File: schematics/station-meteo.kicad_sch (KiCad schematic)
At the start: 4 parts, among them IC2 AHT20, U4 SCD40-D-R2

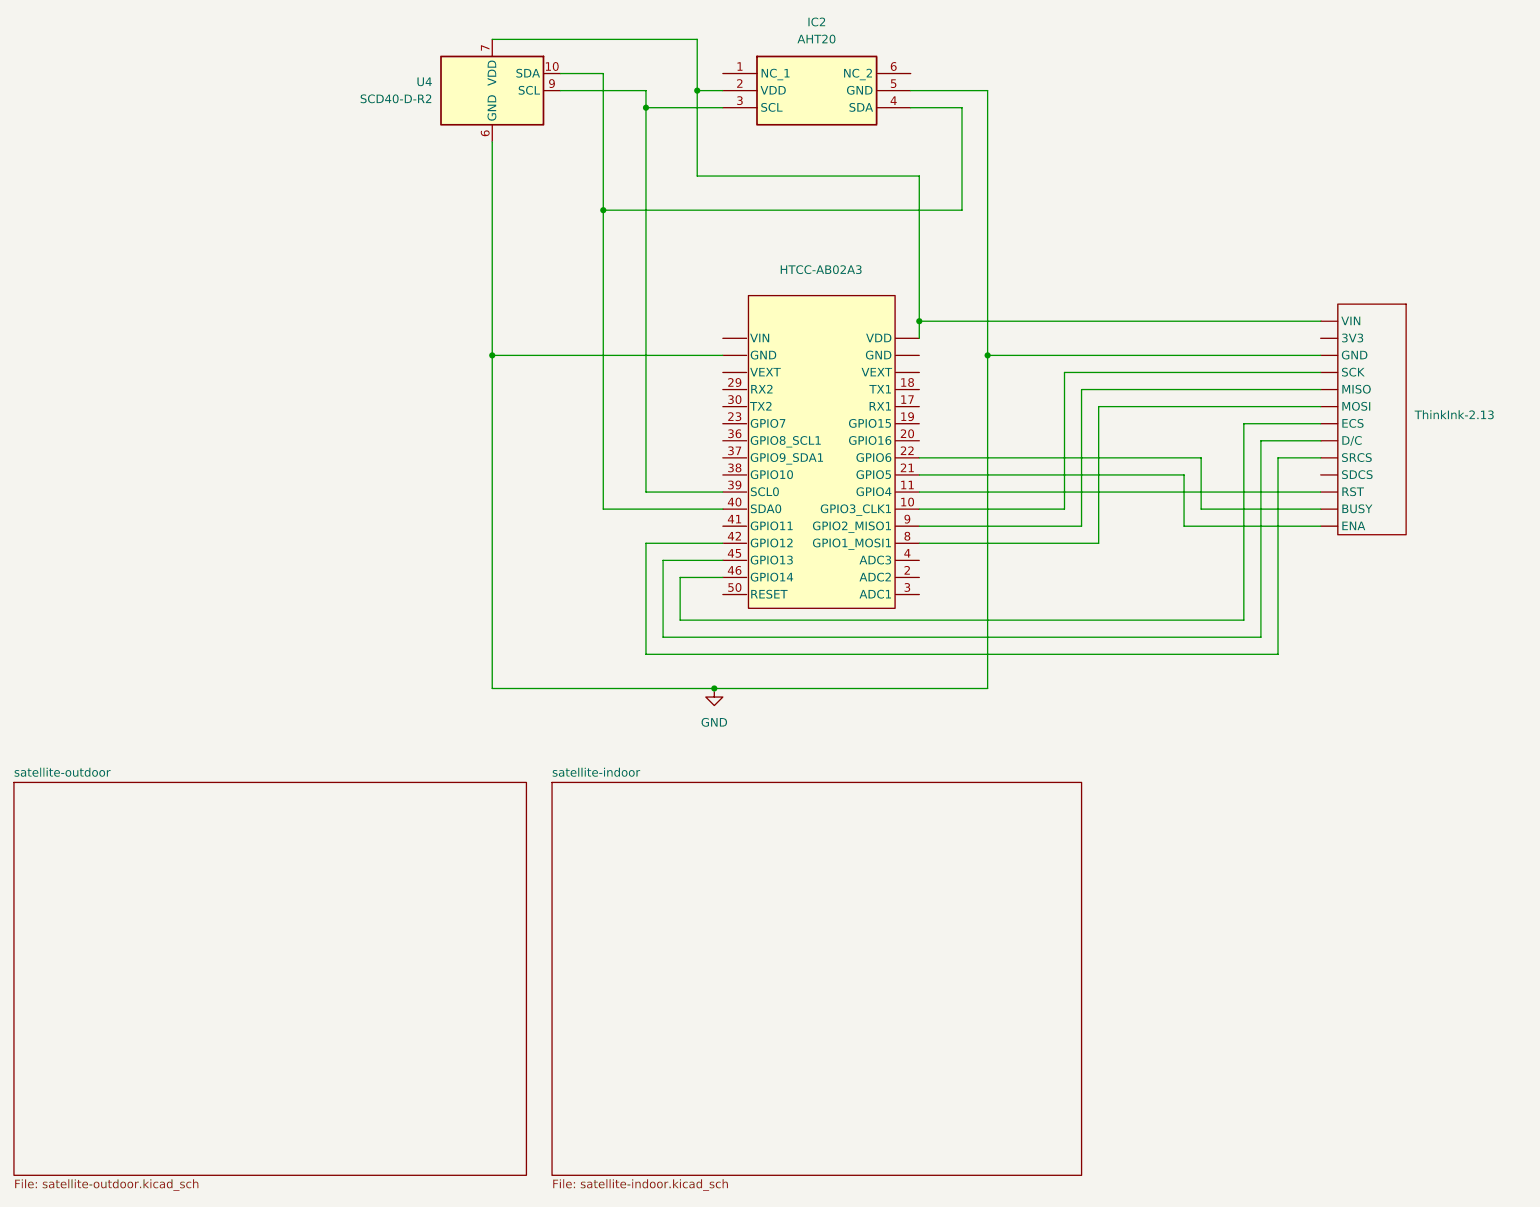
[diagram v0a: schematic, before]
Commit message: Schematics update: use Vext instead of VDD
Vext can be controllled and switched on/off.
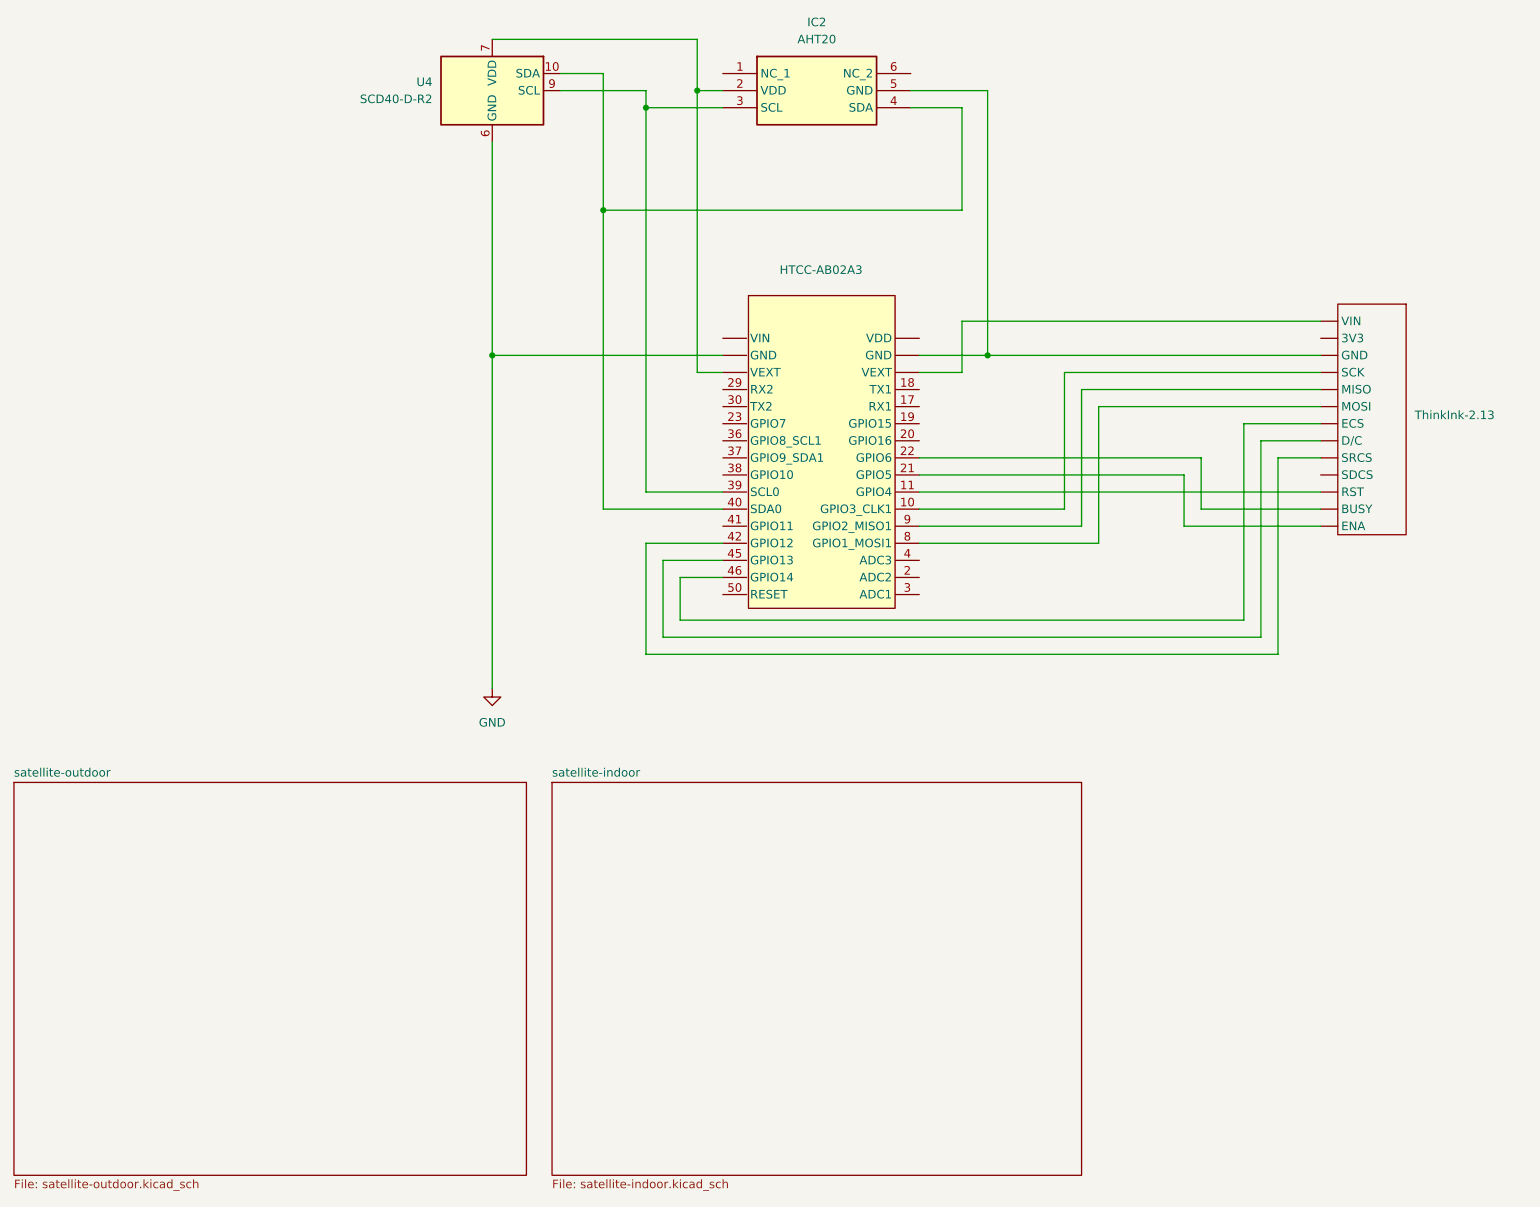
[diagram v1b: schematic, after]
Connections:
- net GND: no longer IC2.5 (GND), ThinkInk-2.13. (VIN)
- net at HTCC-AB02A3. (VIN), IC2.2 (VDD), U4.19 (VDD)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: no longer ThinkInk-2.13. (VIN)
- new net: HTCC-AB02A3. (VIN), ThinkInk-2.13. (VIN)
- new net: HTCC-AB02A3. (VIN), IC2.5 (GND), ThinkInk-2.13. (VIN)
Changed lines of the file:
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@@
-	)
-	(junction
-		(at 120.65 121.92)
-		(diameter 0)
-		(color 0 0 0 0)
-	)
-	(junction
-		(at 151.13 67.31)
-		(diameter 0)
-		(color 0 0 0 0)
 	)
 	(junction
@@
 	(wire
 		(pts
-			(xy 151.13 45.72) (xy 151.13 67.31)
-		)
-		(stroke
-			(width 0)
-			(type default)
-		)
-	)
-	(wire
-		(pts
-			(xy 151.13 67.31) (xy 210.82 67.31)
+			(xy 151.13 72.39) (xy 161.29 72.39)
 		)
 		(stroke
@@
 	(wire
 		(pts
+			(xy 157.48 67.31) (xy 210.82 67.31)
+		)
+		(stroke
+			(width 0)
+			(type default)
+		)
+	)
+	(wire
+		(pts
 			(xy 210.82 95.25) (xy 193.04 95.25)
 		)
@@
 	(wire
 		(pts
-			(xy 161.29 121.92) (xy 120.65 121.92)
-		)
-		(stroke
-			(width 0)
-			(type default)
-		)
-	)
-	(wire
-		(pts
 			(xy 113.03 114.3) (xy 201.93 114.3)
 		)
@@
 	(wire
 		(pts
+			(xy 118.11 33.02) (xy 118.11 74.93)
+		)
+		(stroke
+			(width 0)
+			(type default)
+		)
+	)
+	(wire
+		(pts
 			(xy 161.29 72.39) (xy 210.82 72.39)
 		)
@@
 	(wire
 		(pts
+			(xy 151.13 74.93) (xy 157.48 74.93)
+		)
+		(stroke
+			(width 0)
+			(type default)
+		)
+	)
+	(wire
+		(pts
 			(xy 210.82 87.63) (xy 204.47 87.63)
 		)
@@
 	(wire
 		(pts
-			(xy 151.13 45.72) (xy 118.11 45.72)
-		)
-		(stroke
-			(width 0)
-			(type default)
-		)
-	)
-	(wire
-		(pts
 			(xy 97.79 33.02) (xy 110.49 33.02)
 		)
@@
 	(wire
 		(pts
-			(xy 120.65 121.92) (xy 87.63 121.92)
-		)
-		(stroke
-			(width 0)
-			(type default)
-		)
-	)
-	(wire
-		(pts
-			(xy 118.11 45.72) (xy 118.11 33.02)
-		)
-		(stroke
-			(width 0)
-			(type default)
-		)
-	)
-	(wire
-		(pts
-			(xy 161.29 72.39) (xy 161.29 121.92)
-		)
-		(stroke
-			(width 0)
-			(type default)
-		)
-	)
-	(wire
-		(pts
 			(xy 104.14 95.25) (xy 121.92 95.25)
 		)
@@
 	(wire
 		(pts
-			(xy 151.13 67.31) (xy 151.13 69.85)
-		)
-		(stroke
-			(width 0)
-			(type default)
-		)
-	)
-	(wire
-		(pts
 			(xy 121.92 100.33) (xy 110.49 100.33)
 		)
@@
 	(wire
 		(pts
+			(xy 121.92 74.93) (xy 118.11 74.93)
+		)
+		(stroke
+			(width 0)
+			(type default)
+		)
+	)
+	(wire
+		(pts
 			(xy 177.8 100.33) (xy 177.8 80.01)
+		)
+		(stroke
+			(width 0)
+			(type default)
+		)
+	)
+	(wire
+		(pts
+			(xy 157.48 67.31) (xy 157.48 74.93)
 		)
 		(stroke
@@
 	(symbol
 		(lib_id "power:GND")
-		(at 120.65 121.92 0)
+		(at 87.63 121.92 0)
 		(unit 1)
 		(exclude_from_sim no)
@@
 		(fields_autoplaced yes)
 		(property "Reference" "#PWR03"
-			(at 120.65 128.27 0)
+			(at 87.63 128.27 0)
 			(effects
 				(font
@@
 		)
 		(property "Value" "GND"
-			(at 120.65 127 0)
+			(at 87.63 127 0)
 			(effects
 				(font
@@
 		)
 		(property "Footprint" ""
-			(at 120.65 121.92 0)
+			(at 87.63 121.92 0)
 			(effects
 				(font
@@
 		)
 		(property "Datasheet" ""
-			(at 120.65 121.92 0)
+			(at 87.63 121.92 0)
 			(effects
 				(font
@@
 		)
 		(property "Description" "Power symbol creates a global label with name \"GND\" , ground"
-			(at 120.65 121.92 0)
-			(effects
-				(font
+			(at 87.63 121.92 0)
+			(effects
+				(font

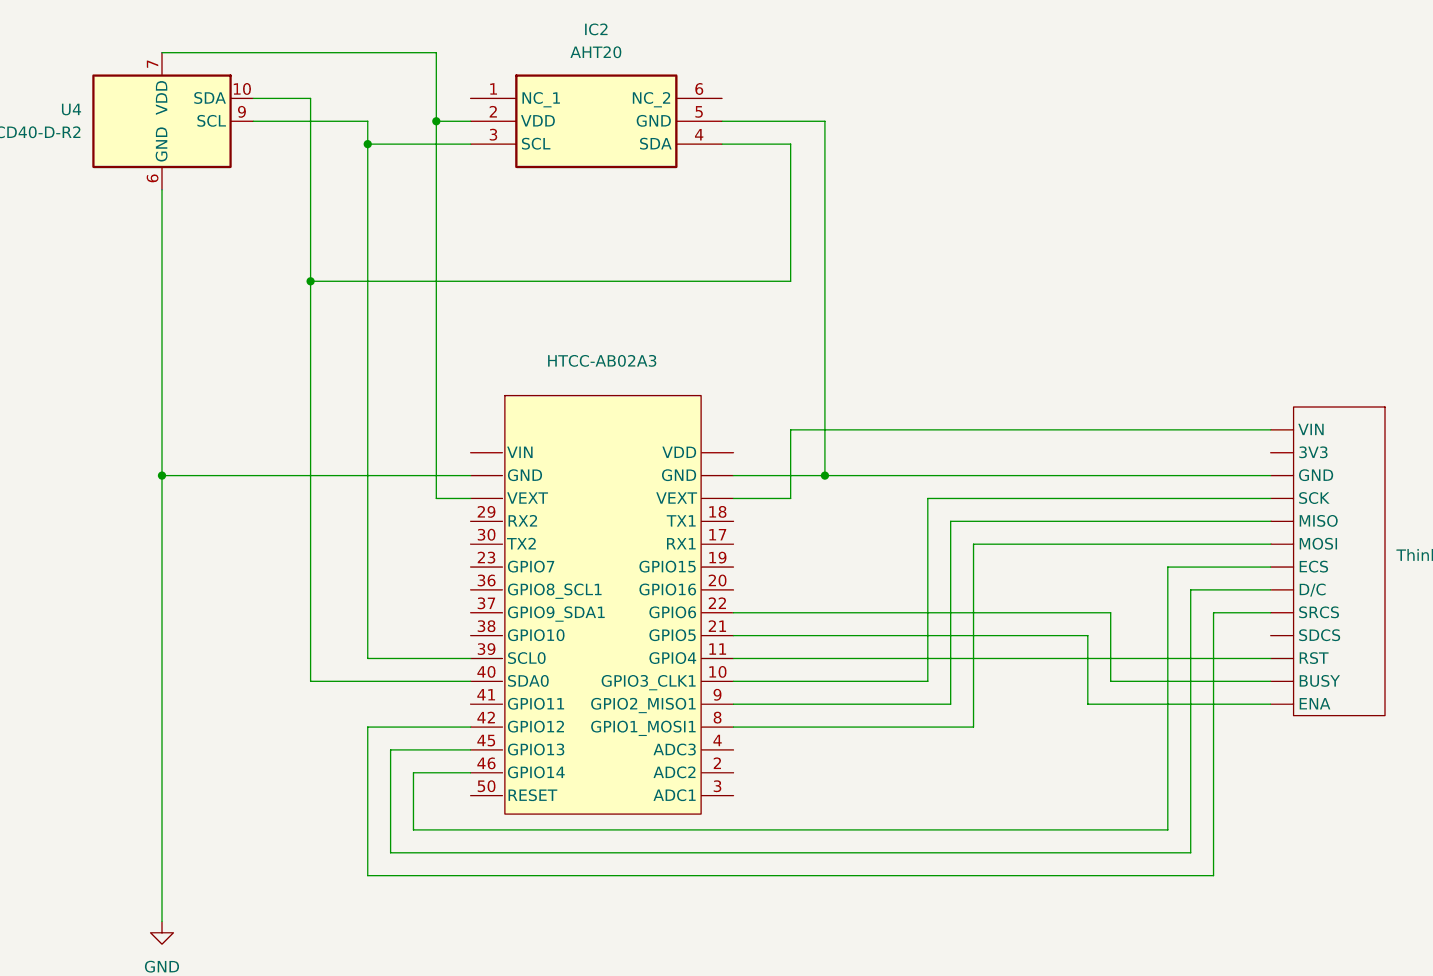
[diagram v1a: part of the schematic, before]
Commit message: Schematics/ add i2c pullups on outdoor sat.
20ko should do the trick.
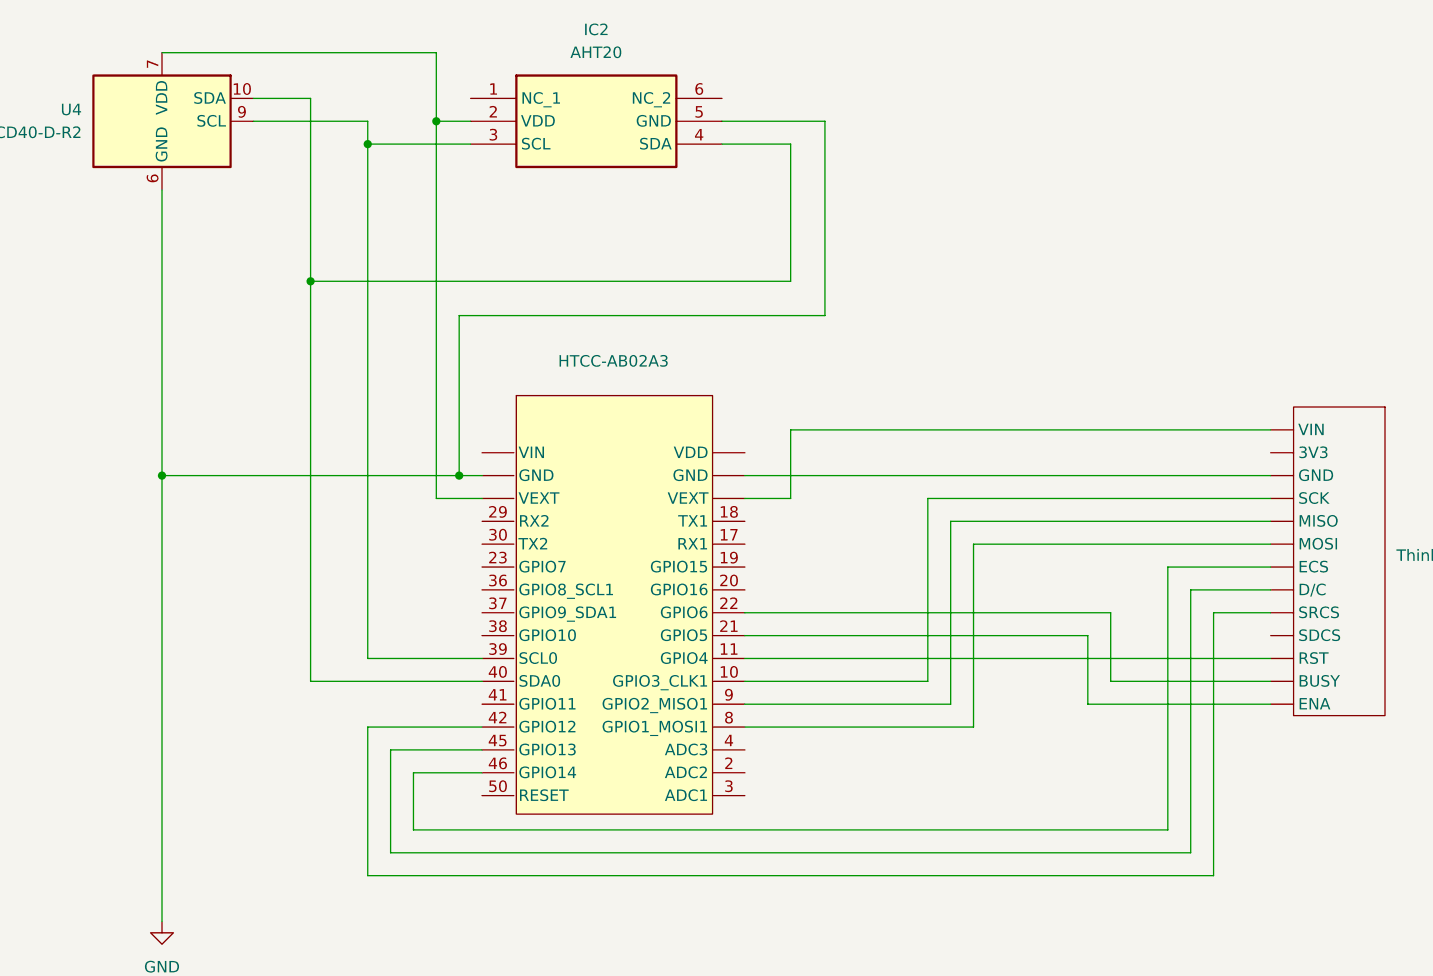
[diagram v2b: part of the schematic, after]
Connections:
- net GND: now also IC2.5 (GND)
- net at ThinkInk-2.13. (VIN): no longer HTCC-AB02A3. (VIN)
- new net: HTCC-AB02A3. (VIN), ThinkInk-2.13. (VIN) (x2)
- now unconnected: ThinkInk-2.13. (VIN)
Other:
- moved on the sheet: HTCC-AB02A3
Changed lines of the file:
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@@
+	)
+	(junction
+		(at 120.65 72.39)
+		(diameter 0)
+		(color 0 0 0 0)
 	)
 	(junction
@@
 		(color 0 0 0 0)
 	)
-	(junction
-		(at 161.29 72.39)
-		(diameter 0)
-		(color 0 0 0 0)
-	)
-	(wire
-		(pts
-			(xy 151.13 72.39) (xy 161.29 72.39)
-		)
-		(stroke
-			(width 0)
-			(type default)
-		)
-	)
 	(wire
 		(pts
@@
 	(wire
 		(pts
-			(xy 110.49 92.71) (xy 121.92 92.71)
+			(xy 110.49 92.71) (xy 123.19 92.71)
 		)
 		(stroke
@@
 	(wire
 		(pts
-			(xy 121.92 102.87) (xy 113.03 102.87)
+			(xy 123.19 102.87) (xy 113.03 102.87)
 		)
 		(stroke
@@
 	(wire
 		(pts
+			(xy 120.65 54.61) (xy 161.29 54.61)
+		)
+		(stroke
+			(width 0)
+			(type default)
+		)
+	)
+	(wire
+		(pts
 			(xy 157.48 50.8) (xy 104.14 50.8)
 		)
@@
 	(wire
 		(pts
-			(xy 193.04 87.63) (xy 151.13 87.63)
+			(xy 193.04 87.63) (xy 152.4 87.63)
 		)
 		(stroke
@@
 	(wire
 		(pts
-			(xy 161.29 72.39) (xy 210.82 72.39)
-		)
-		(stroke
-			(width 0)
-			(type default)
-		)
-	)
-	(wire
-		(pts
-			(xy 151.13 74.93) (xy 157.48 74.93)
+			(xy 152.4 72.39) (xy 210.82 72.39)
+		)
+		(stroke
+			(width 0)
+			(type default)
+		)
+	)
+	(wire
+		(pts
+			(xy 120.65 72.39) (xy 123.19 72.39)
+		)
+		(stroke
+			(width 0)
+			(type default)
+		)
+	)
+	(wire
+		(pts
+			(xy 120.65 72.39) (xy 120.65 54.61)
+		)
+		(stroke
+			(width 0)
+			(type default)
+		)
+	)
+	(wire
+		(pts
+			(xy 152.4 74.93) (xy 157.48 74.93)
 		)
 		(stroke
@@
 	(wire
 		(pts
-			(xy 151.13 97.79) (xy 175.26 97.79)
+			(xy 152.4 97.79) (xy 175.26 97.79)
 		)
 		(stroke
@@
 	(wire
 		(pts
-			(xy 87.63 72.39) (xy 121.92 72.39)
+			(xy 87.63 72.39) (xy 120.65 72.39)
 		)
 		(stroke
@@
 	(wire
 		(pts
-			(xy 161.29 33.02) (xy 161.29 72.39)
+			(xy 161.29 33.02) (xy 161.29 54.61)
 		)
 		(stroke
@@
 	(wire
 		(pts
-			(xy 151.13 90.17) (xy 190.5 90.17)
+			(xy 152.4 90.17) (xy 190.5 90.17)
 		)
 		(stroke
@@
 	(wire
 		(pts
-			(xy 115.57 105.41) (xy 121.92 105.41)
-		)
-		(stroke
-			(width 0)
-			(type default)
-		)
-	)
-	(wire
-		(pts
-			(xy 104.14 95.25) (xy 121.92 95.25)
+			(xy 115.57 105.41) (xy 123.19 105.41)
+		)
+		(stroke
+			(width 0)
+			(type default)
+		)
+	)
+	(wire
+		(pts
+			(xy 104.14 95.25) (xy 123.19 95.25)
 		)
 		(stroke
@@
 	(wire
 		(pts
-			(xy 151.13 100.33) (xy 177.8 100.33)
-		)
-		(stroke
-			(width 0)
-			(type default)
-		)
-	)
-	(wire
-		(pts
-			(xy 151.13 92.71) (xy 210.82 92.71)
-		)
-		(stroke
-			(width 0)
-			(type default)
-		)
-	)
-	(wire
-		(pts
-			(xy 151.13 95.25) (xy 172.72 95.25)
+			(xy 152.4 100.33) (xy 177.8 100.33)
+		)
+		(stroke
+			(width 0)
+			(type default)
+		)
+	)
+	(wire
+		(pts
+			(xy 152.4 92.71) (xy 210.82 92.71)
+		)
+		(stroke
+			(width 0)
+			(type default)
+		)
+	)
+	(wire
+		(pts
+			(xy 152.4 95.25) (xy 172.72 95.25)
 		)
 		(stroke
@@
 	(wire
 		(pts
-			(xy 121.92 100.33) (xy 110.49 100.33)
-		)
-		(stroke
-			(width 0)
-			(type default)
-		)
-	)
-	(wire
-		(pts
-			(xy 121.92 74.93) (xy 118.11 74.93)
+			(xy 123.19 100.33) (xy 110.49 100.33)
+		)
+		(stroke
+			(width 0)
+			(type default)
+		)
+	)
+	(wire
+		(pts
+			(xy 123.19 74.93) (xy 118.11 74.93)
 		)
 		(stroke
@@
 	(symbol
 		(lib_id "meteostation_lib:HTCC-AB02")
-		(at 134.62 60.96 0)
+		(at 135.89 60.96 0)
 		(unit 1)
 		(exclude_from_sim no)
@@
 		(fields_autoplaced yes)
 		(property "Reference" "HTCC-AB02A3"
-			(at 136.525 59.69 0)
+			(at 137.795 59.69 0)
 			(effects
 				(font
@@
 		)
 		(property "Value" "~"
-			(at 136.525 62.23 0)
+			(at 137.795 62.23 0)
 			(effects
 				(font
@@
 		)
 		(property "Footprint" ""
-			(at 134.62 60.96 0)
+			(at 135.89 60.96 0)
 			(effects
 				(font
@@
 		)
 		(property "Datasheet" ""
-			(at 134.62 60.96 0)
+			(at 135.89 60.96 0)
 			(effects
 				(font
@@
 		)
 		(property "Description" ""
-			(at 134.62 60.96 0)
-			(effects
-				(font
+			(at 135.89 60.96 0)
+			(effects
+				(font
